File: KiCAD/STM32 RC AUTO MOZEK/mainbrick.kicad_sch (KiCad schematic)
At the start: 29 parts, among them J8 Conn_01x03_Socket, U10 ACS712xLCTR-20A, U11 ACS712xLCTR-20A, U13 STM32F030C8Tx, U2 SHT4x, U4 ACS712xLCTR-20A, U5 NRF24L01_Breakout, U7 ACS712xLCTR-20A, U8 ACS712xLCTR-20A, U9 ACS712xLCTR-20A, Y1 Crystal, Y2 Crystal

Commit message: i dont know
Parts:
- removed J8: Conn_01x03_Socket, Connector_Wire:SolderWire-0.5sqmm_1x03_P4.6mm_D0.9mm_OD2.1mm_Relief, symbol Connector:Conn_01x03_Socket
- added J8: Conn_01x05_Socket, Connector_Wire:SolderWire-0.5sqmm_1x05_P4.8mm_D0.9mm_OD2.3mm_Relief, symbol Connector:Conn_01x05_Socket
- added JP8: SolderJumper_3_Open, Jumper:SolderJumper-3_P1.3mm_Open_RoundedPad1.0x1.5mm_NumberLabels, symbol Jumper:SolderJumper_3_Open
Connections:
- net GND: now also J8.1 (Pin_1)
- net at U13.20 (PB2): now also JP8.2 (C); no longer U5.4 (~{CSN})
- net at JP3.1 (A): now also J8.3 (Pin_3)
- net at JP1.1 (A): now also J8.5 (Pin_5)
- net at JP2.1 (A): now also J8.4 (Pin_4)
- new net: J8.2 (Pin_2), JP8.1 (A)
- new net: JP8.3 (B), U5.4 (~{CSN})
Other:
- moved on the sheet: JP2, JP3

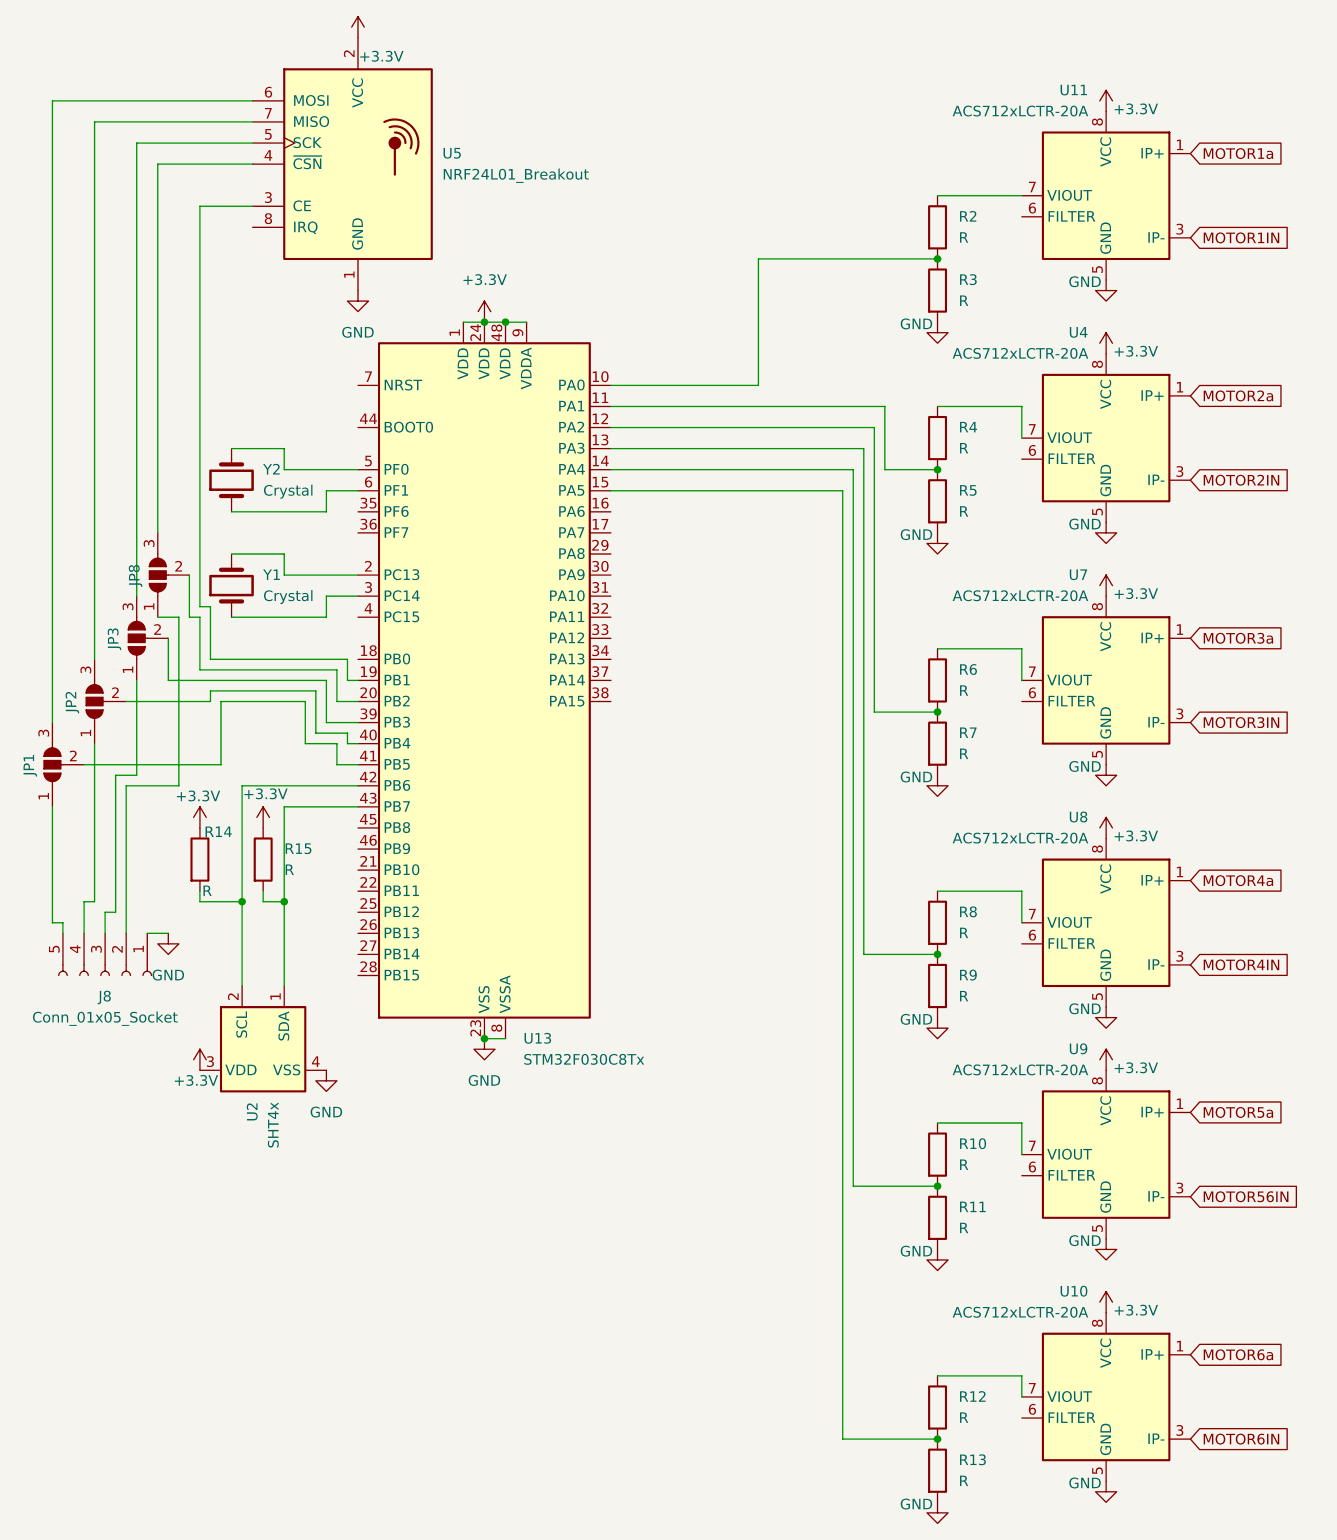
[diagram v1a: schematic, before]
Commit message: Motor power brick implementation
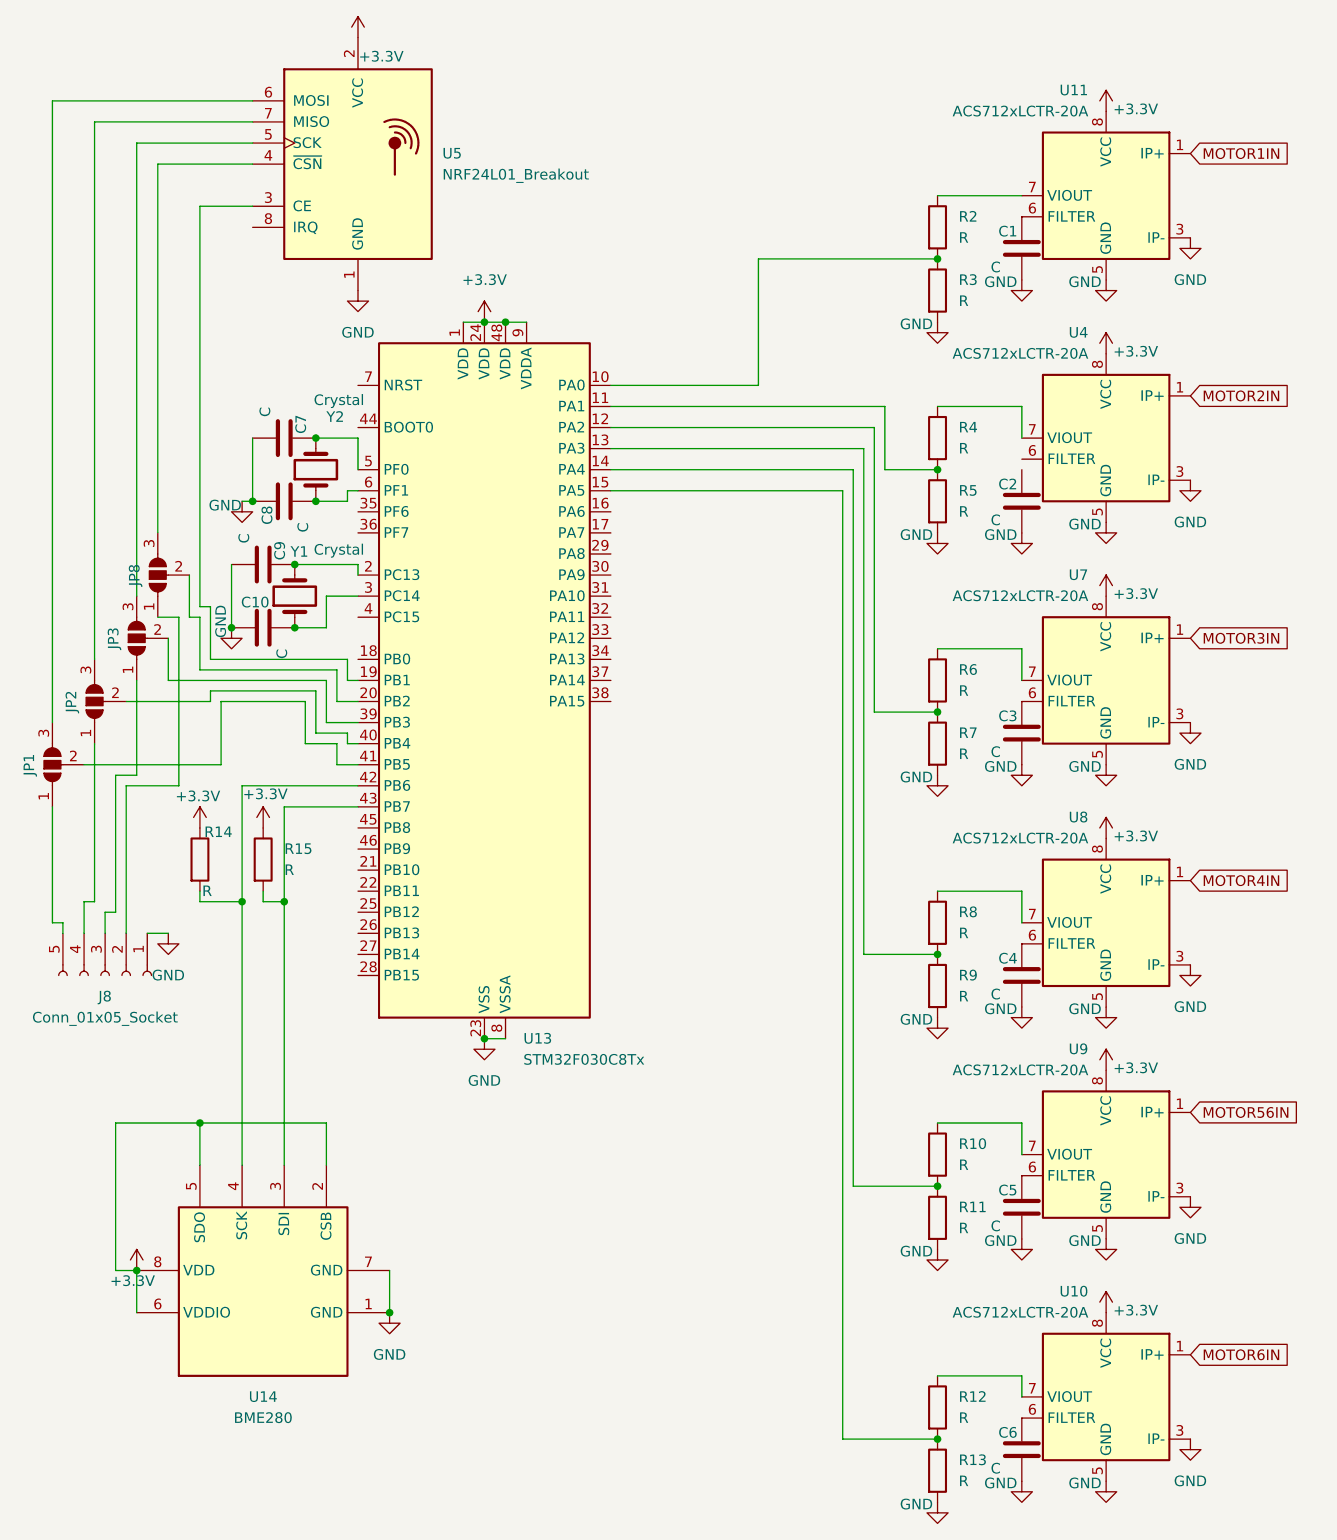
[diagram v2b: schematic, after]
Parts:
- removed U2: SHT4x, Sensor_Humidity:Sensirion_DFN-4_1.5x1.5mm_P0.8mm_SHT4x_NoCentralPad, symbol Sensor_Humidity:SHT4x
- added C1, C10, C2, C3, C4, C5, C6, C7, C8, C9: C, symbol Device:C
- added U14: BME280, Package_LGA:Bosch_LGA-8_2.5x2.5mm_P0.65mm_ClockwisePinNumbering, symbol Sensor:BME280
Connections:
- net MOTOR1a is gone; now on net MOTOR1IN: U11.1 (IP+), U11.2 (IP+)
- net MOTOR2a is gone; now on net MOTOR2IN: U4.1 (IP+), U4.2 (IP+)
- net MOTOR3a is gone; now on net MOTOR3IN: U7.1 (IP+), U7.2 (IP+)
- net MOTOR4a is gone; now on net MOTOR4IN: U8.1 (IP+), U8.2 (IP+)
- net MOTOR5a is gone; now on net MOTOR56IN: U9.1 (IP+), U9.2 (IP+)
- net MOTOR6a is gone; now on net MOTOR6IN: U10.1 (IP+), U10.2 (IP+)
- net +3.3V: now also U14.2 (CSB), U14.5 (SDO), U14.6 (VDDIO), U14.8 (VDD)
- net GND: now also U10.3 (IP-), U10.4 (IP-), U11.3 (IP-), U11.4 (IP-), U4.3 (IP-), U4.4 (IP-), U7.3 (IP-), U7.4 (IP-), U8.3 (IP-), U8.4 (IP-), U9.3 (IP-), U9.4 (IP-), C1.2, C10.1, C2.2, C3.2, C4.2, C5.2, C6.2, C7.2, C8.1, C9.2, U14.1 (GND), U14.7 (GND)
- net MOTOR1IN: no longer U11.3 (IP-), U11.4 (IP-)
- net MOTOR2IN: no longer U4.3 (IP-), U4.4 (IP-)
- net MOTOR3IN: no longer U7.3 (IP-), U7.4 (IP-)
- net MOTOR4IN: no longer U8.3 (IP-), U8.4 (IP-)
- net MOTOR56IN: no longer U9.3 (IP-), U9.4 (IP-)
- net MOTOR6IN: no longer U10.3 (IP-), U10.4 (IP-)
- net at R15.2, U13.43 (PB7): now also U14.3 (SDI)
- net at R14.2, U13.42 (PB6): now also U14.4 (SCK)
- net at U13.3 (PC14), Y1.1: now also C10.2
- net at U13.2 (PC13), Y1.2: now also C9.1
- net at U8.6 (FILTER): now also C4.1
- net at U11.6 (FILTER): now also C1.1
- net at U9.6 (FILTER): now also C5.1
- net at U13.6 (PF1), Y2.1: now also C8.2
- net at U13.5 (PF0), Y2.2: now also C7.1
- net at U10.6 (FILTER): now also C6.1
- net at U7.6 (FILTER): now also C3.1
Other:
- moved on the sheet: Y1, Y2

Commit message: .
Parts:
- C1, C2, C3, C4, C5, C6: footprint (none) -> Capacitor_SMD:C_0805_2012Metric_Pad1.18x1.45mm_HandSolder
- C10, C7, C8, C9: value C -> 12,5pF; footprint (none) -> Capacitor_SMD:C_0805_2012Metric_Pad1.18x1.45mm_HandSolder
- R10, R11, R12, R13, R14, R15, R2, R3, R4, R5, R6, R7, R8, R9: footprint (none) -> Resistor_SMD:R_0805_2012Metric_Pad1.20x1.40mm_HandSolder
- Y1: value Crystal -> 32.786KHz; footprint (none) -> Crystal:Crystal_DS26_D2.0mm_L6.0mm_Horizontal
- Y2: value Crystal -> 25MHz; footprint (none) -> Crystal:Crystal_SMD_HC49-SD
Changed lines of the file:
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@@
 	)
 	(junction
-		(at 129.54 154.94)
+		(at 52.07 87.63)
 		(diameter 0)
 		(color 0 0 0 0)
 	)
 	(junction
-		(at 50.8 120.65)
+		(at 129.54 154.94)
 		(diameter 0)
 		(color 0 0 0 0)
 	)
 	(junction
-		(at 52.07 87.63)
+		(at 50.8 120.65)
 		(diameter 0)
 		(color 0 0 0 0)
@@
 	)
 	(junction
-		(at 52.07 80.01)
-		(diameter 0)
-		(color 0 0 0 0)
-	)
-	(junction
 		(at 63.5 170.18)
 		(diameter 0)
@@
 	)
 	(junction
+		(at 52.07 80.01)
+		(diameter 0)
+		(color 0 0 0 0)
+	)
+	(junction
 		(at 129.54 185.42)
 		(diameter 0)
@@
 			)
 		)
-		(property "Footprint" ""
+		(property "Footprint" "Resistor_SMD:R_0805_2012Metric_Pad1.20x1.40mm_HandSolder"
 			(at 127.762 101.6 90)
 			(effects
@@
 			)
 		)
-		(property "Footprint" ""
+		(property "Footprint" "Capacitor_SMD:C_0805_2012Metric_Pad1.18x1.45mm_HandSolder"
 			(at 138.7348 161.29 0)
 			(effects
@@
 	)
 	(symbol
-		(lib_id "Device:Crystal")
-		(at 52.07 83.82 90)
-		(unit 1)
-		(exclude_from_sim no)
-		(in_bom yes)
-		(on_board yes)
-		(dnp no)
-		(property "Reference" "Y1"
-			(at 51.562 78.486 90)
-			(effects
-				(font
-					(size 1.27 1.27)
-				)
-				(justify right)
-			)
-		)
-		(property "Value" "Crystal"
-			(at 54.356 78.232 90)
-			(effects
-				(font
-					(size 1.27 1.27)
-				)
-				(justify right)
-			)
-		)
-		(property "Footprint" ""
-			(at 52.07 83.82 0)
-			(effects
-				(font
-					(size 1.27 1.27)
-				)
-				(hide yes)
-			)
-		)
-		(property "Datasheet" "~"
-			(at 52.07 83.82 0)
-			(effects
-				(font
-					(size 1.27 1.27)
-				)
-				(hide yes)
-			)
-		)
-		(property "Description" "Two pin crystal"
-			(at 52.07 83.82 0)
-			(effects
-				(font
-					(size 1.27 1.27)
-				)
-				(hide yes)
-			)
-		)
-		(pin "2"
-		)
-		(pin "1"
-		)
-		(instances
-			(project ""
-				(path "/6e2a7673-a3dd-4427-9adf-f28c7cc113a0/51c8adc8-39e6-4ff6-9e54-3a41925bf3db"
-					(reference "Y1")
-					(unit 1)
-				)
-			)
-		)
-	)
-	(symbol
 		(lib_id "Device:R")
 		(at 129.54 189.23 0)
@@
 			)
 		)
-		(property "Footprint" ""
+		(property "Footprint" "Resistor_SMD:R_0805_2012Metric_Pad1.20x1.40mm_HandSolder"
 			(at 127.762 189.23 90)
 			(effects
@@
 			)
 		)
-		(property "Footprint" ""
+		(property "Footprint" "Capacitor_SMD:C_0805_2012Metric_Pad1.18x1.45mm_HandSolder"
 			(at 138.7348 76.2 0)
 			(effects
@@
 		(dnp no)
 		(property "Reference" "C7"
-			(at 52.832 64.262 0)
+			(at 50.292 61.468 90)
 			(effects
 				(font
@@
 			)
 		)
-		(property "Value" "C"
-			(at 48.514 62.23 0)
+		(property "Value" "12,5pF"
+			(at 42.672 63.246 90)
 			(effects
 				(font
@@
 			)
 		)
-		(property "Footprint" ""
+		(property "Footprint" "Capacitor_SMD:C_0805_2012Metric_Pad1.18x1.45mm_HandSolder"
 			(at 46.99 63.8048 0)
 			(effects
@@
 			)
 		)
-		(property "Value" "C"
-			(at 45.974 77.47 0)
+		(property "Value" "12,5pF"
+			(at 42.926 76.708 90)
 			(effects
 				(font
@@
 			)
 		)
-		(property "Footprint" ""
+		(property "Footprint" "Capacitor_SMD:C_0805_2012Metric_Pad1.18x1.45mm_HandSolder"
 			(at 44.45 79.0448 0)
 			(effects
@@
 	)
 	(symbol
+		(lib_id "Device:Crystal")
+		(at 52.07 83.82 90)
+		(unit 1)
+		(exclude_from_sim no)
+		(in_bom yes)
+		(on_board yes)
+		(dnp no)
+		(property "Reference" "Y1"
+			(at 55.118 76.454 90)
+			(effects
+				(font
+					(size 1.27 1.27)
+				)
+				(justify right)
+			)
+		)
+		(property "Value" "32.786KHz"
+			(at 51.562 78.486 90)
+			(effects
+				(font
+					(size 1.27 1.27)
+				)
+				(justify right)
+			)
+		)
+		(property "Footprint" "Crystal:Crystal_DS26_D2.0mm_L6.0mm_Horizontal"
+			(at 52.07 83.82 0)
+			(effects
+				(font
+					(size 1.27 1.27)
+				)
+				(hide yes)
+			)
+		)
+		(property "Datasheet" "~"
+			(at 52.07 83.82 0)
+			(effects
+				(font
+					(size 1.27 1.27)
+				)
+				(hide yes)
+			)
+		)
+		(property "Description" "Two pin crystal"
+			(at 52.07 83.82 0)
+			(effects
+				(font
+					(size 1.27 1.27)
+				)
+				(hide yes)
+			)
+		)
+		(pin "2"
+		)
+		(pin "1"
+		)
+		(instances
+			(project "STM32 RC AUTO MOZEK"
+				(path "/6e2a7673-a3dd-4427-9adf-f28c7cc113a0/51c8adc8-39e6-4ff6-9e54-3a41925bf3db"
+					(reference "Y1")
+					(unit 1)
+				)
+			)
+		)
+	)
+	(symbol
 		(lib_id "Device:R")
 		(at 129.54 181.61 0)
@@
 			)
 		)
-		(property "Footprint" ""
+		(property "Footprint" "Resistor_SMD:R_0805_2012Metric_Pad1.20x1.40mm_HandSolder"
 			(at 127.762 181.61 90)
 			(effects
@@
 			)
 		)
-		(property "Footprint" ""
+		(property "Footprint" "Resistor_SMD:R_0805_2012Metric_Pad1.20x1.40mm_HandSolder"
 			(at 38.862 115.57 90)
 			(effects
@@
 			)
 		)
-		(property "Footprint" ""
+		(property "Footprint" "Capacitor_SMD:C_0805_2012Metric_Pad1.18x1.45mm_HandSolder"
 			(at 138.7348 45.72 0)
 			(effects
@@
 			)
 		)
-		(property "Value" "C"
-			(at 53.086 74.93 0)
+		(property "Value" "12,5pF"
+			(at 58.928 73.914 90)
 			(effects
 				(font
@@
 			)
 		)
-		(property "Footprint" ""
+		(property "Footprint" "Capacitor_SMD:C_0805_2012Metric_Pad1.18x1.45mm_HandSolder"
 			(at 54.61 73.3552 0)
 			(effects
@@
 			)
 		)
-		(property "Footprint" ""
+		(property "Footprint" "Capacitor_SMD:C_0805_2012Metric_Pad1.18x1.45mm_HandSolder"
 			(at 138.7348 190.5 0)
 			(effects
@@
 			)
 		)
-		(property "Footprint" ""
+		(property "Footprint" "Capacitor_SMD:C_0805_2012Metric_Pad1.18x1.45mm_HandSolder"
 			(at 138.7348 133.35 0)
 			(effects
@@
 			)
 		)
-		(property "Value" "C"
-			(at 50.546 90.17 0)
+		(property "Value" "12,5pF"
+			(at 56.388 89.408 90)
 			(effects
 				(font
@@
 			)
 		)
-		(property "Footprint" ""
+		(property "Footprint" "Capacitor_SMD:C_0805_2012Metric_Pad1.18x1.45mm_HandSolder"
 			(at 52.07 88.5952 0)
 			(effects
@@
 			)
 		)
-		(property "Footprint" ""
+		(property "Footprint" "Resistor_SMD:R_0805_2012Metric_Pad1.20x1.40mm_HandSolder"
 			(at 127.762 39.37 90)
 			(effects
@@
 		(dnp no)
 		(property "Reference" "Y2"
-			(at 55.88 62.23 90)
+			(at 56.896 66.04 90)
 			(effects
 				(font
@@
 			)
 		)
-		(property "Value" "Crystal"
-			(at 54.356 60.198 90)
+		(property "Value" "25MHz"
+			(at 52.324 63.5 90)
 			(effects
 				(font
@@
 			)
 		)
-		(property "Footprint" ""
+		(property "Footprint" "Crystal:Crystal_SMD_HC49-SD"
 			(at 54.61 68.58 0)
 			(effects
@@
 			)
 		)
-		(property "Footprint" ""
+		(property "Footprint" "Resistor_SMD:R_0805_2012Metric_Pad1.20x1.40mm_HandSolder"
 			(at 127.762 151.13 90)
 			(effects
@@
 			)
 		)
-		(property "Footprint" ""
+		(property "Footprint" "Resistor_SMD:R_0805_2012Metric_Pad1.20x1.40mm_HandSolder"
 			(at 127.762 93.98 90)
 			(effects
@@
 			)
 		)
-		(property "Footprint" ""
+		(property "Footprint" "Capacitor_SMD:C_0805_2012Metric_Pad1.18x1.45mm_HandSolder"
 			(at 138.7348 104.14 0)
 			(effects
@@
 			)
 		)
-		(property "Footprint" ""
+		(property "Footprint" "Resistor_SMD:R_0805_2012Metric_Pad1.20x1.40mm_HandSolder"
 			(at 127.762 158.75 90)
 			(effects
@@
 			)
 		)
-		(property "Footprint" ""
+		(property "Footprint" "Resistor_SMD:R_0805_2012Metric_Pad1.20x1.40mm_HandSolder"
 			(at 46.482 115.57 90)
 			(effects
@@
 			)
 		)
-		(property "Footprint" ""
+		(property "Footprint" "Resistor_SMD:R_0805_2012Metric_Pad1.20x1.40mm_HandSolder"
 			(at 127.762 72.39 90)
 			(effects
@@
 			)
 		)
-		(property "Footprint" ""
+		(property "Footprint" "Resistor_SMD:R_0805_2012Metric_Pad1.20x1.40mm_HandSolder"
 			(at 127.762 123.19 90)
 			(effects
@@
 			)
 		)
-		(property "Footprint" ""
+		(property "Footprint" "Resistor_SMD:R_0805_2012Metric_Pad1.20x1.40mm_HandSolder"
 			(at 127.762 46.99 90)
 			(effects
@@
 			)
 		)
-		(property "Footprint" ""
+		(property "Footprint" "Resistor_SMD:R_0805_2012Metric_Pad1.20x1.40mm_HandSolder"
 			(at 127.762 130.81 90)
 			(effects
@@
 			)
 		)
-		(property "Footprint" ""
+		(property "Footprint" "Resistor_SMD:R_0805_2012Metric_Pad1.20x1.40mm_HandSolder"
 			(at 127.762 64.77 90)
 			(effects
